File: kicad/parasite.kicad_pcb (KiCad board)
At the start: 2 copper layers, 22 x 110.4 mm, 34 parts, among them Q1 MMBT3904, Q2 MMBT3904, Q3 AO3407, U1 E73-2G4M08S1C-52840, U2 SHTC3, Y1 32.768kHz

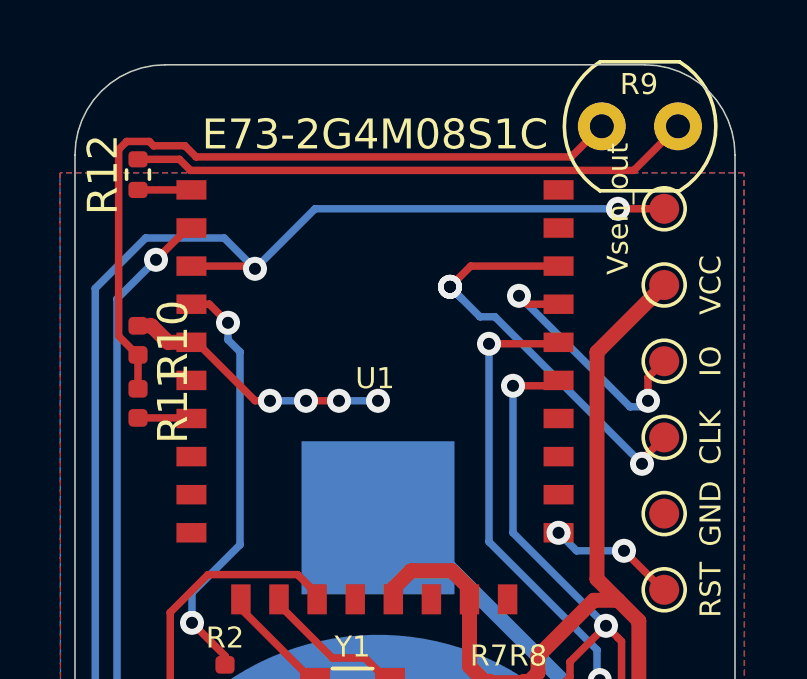
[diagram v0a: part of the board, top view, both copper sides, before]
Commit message: simplify voltage divider
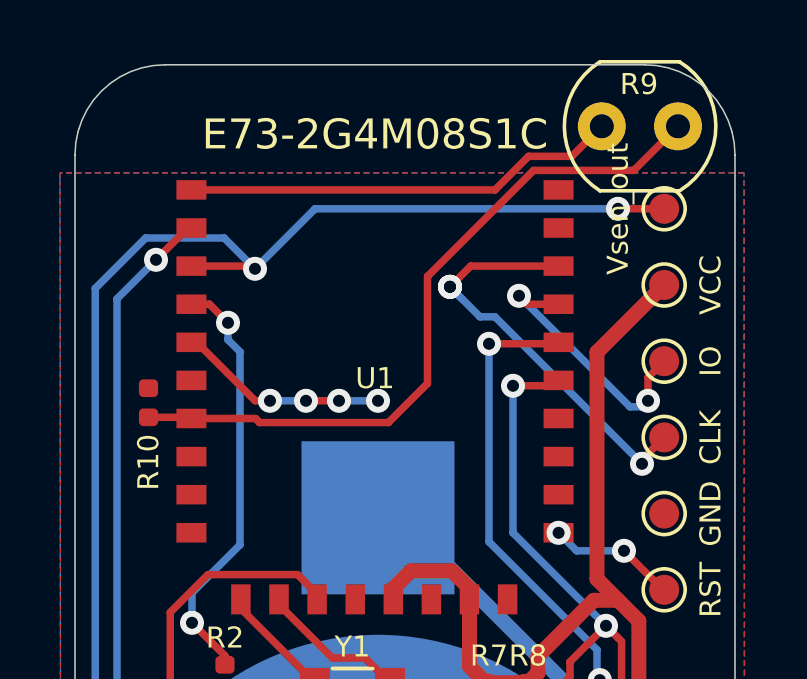
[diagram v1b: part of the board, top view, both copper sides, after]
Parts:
- removed R11: 220, Resistor_SMD:R_0402_1005Metric
- removed R12: 10k, Resistor_SMD:R_0402_1005Metric
- R10: value 2k -> 10k
- moved R10 2.11 mm to (59.5, 38.3)
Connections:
- R10 pad 2: Net-(R10-Pad2) -> /PHOTO_OUT
- R9 pad 1: Net-(R12-Pad2) -> /PHOTO_OUT
- R9 pad 2: Net-(R10-Pad2) -> /PHOTO_V
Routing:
- net Net-(R10-Pad2): track 25.1 -> 0.00 mm
- net /PHOTO_OUT: track 1.79 -> 23.9 mm
- net Net-(R12-Pad2): track 18.8 -> 0.00 mm
- net /PHOTO_V: track 1.78 -> 14.8 mm
- net GND: track 17.5 -> 15.5 mm
